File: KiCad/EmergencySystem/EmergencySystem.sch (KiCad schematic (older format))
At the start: 15 parts, among them K1 HE1AN-S-DC12V, K2 HE1AN-S-DC12V, M1 Left_Motor, M2 Right_Motor, U1 T3_EmergencyLight_RED, U2 T3_EmergencyLight_BLUE, U3 T3_EmergencyLight_AMBER, U4 e-Boot_BuckConverter, U5 Elegoo_4RelayModule, U6 Feather_32u4_RFM95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

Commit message: Finalized the initial version of the emergency transmitter/receiver schematic. PDF export was also uploaded.
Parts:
- removed BT1, BT2: Motor_Battery, symbol Device:Battery_Cell
- removed U7: e-Boot_BuckConverter, symbol RoboBoat_Parts:e-Boot_BuckConverter
- added AE1, AE2: Adafruit_900MHz_Antenna, symbol Device:Antenna
- added R1, R2: 5k, symbol Device:R_US
- added SW1: E-StopButton01, symbol Switch:SW_Push_Open
- added SW2: E-StopButton02, symbol Switch:SW_Push_Open
- added SW3, SW4: ON/OFF_Switch, symbol Switch:SW_SPST
- added SW5: E-Stop_Switch, symbol Switch:SW_SPST
- added U10, U7: Adafruit_2200mAh_LiPo, symbol RoboBoat_Parts:Adafruit_2200mAh_LiPo
- added U11: OLED_I2C_Display, symbol RoboBoat_Parts:OLED_I2C_Display
- added U8: Feather_32u4_RFM95, symbol AdafruitBoards:Feather_32u4_RFM95
- added U9: e-Boot_BuckConverter, symbol RoboBoat_Parts:e-Boot_BuckConverter
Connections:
- net labels added: +12V, +3V3_Rx, +3V3_Tx, +5V_Rx, +BATT_14.8V, +BATT_22.2V, -BATT_22.2V, -BATT__14.8V, GND_Rx, GND_Tx, Rx_BatteryMonitor, Tx_BatteryMonitor
- net labels removed: +5V, +BATT, -BATT, GND
- wire segments 81 -> 144
- no-connect marks 16 -> 53
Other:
- note added: "Emergency Receiver"
- note added: "Emergency Transmitter"
- note removed: "22.2V 5S LiPO"
- moved on the sheet: CB1, CB2, K1, K2, M1, M2, U1, U2, U3, U4, U5, U6

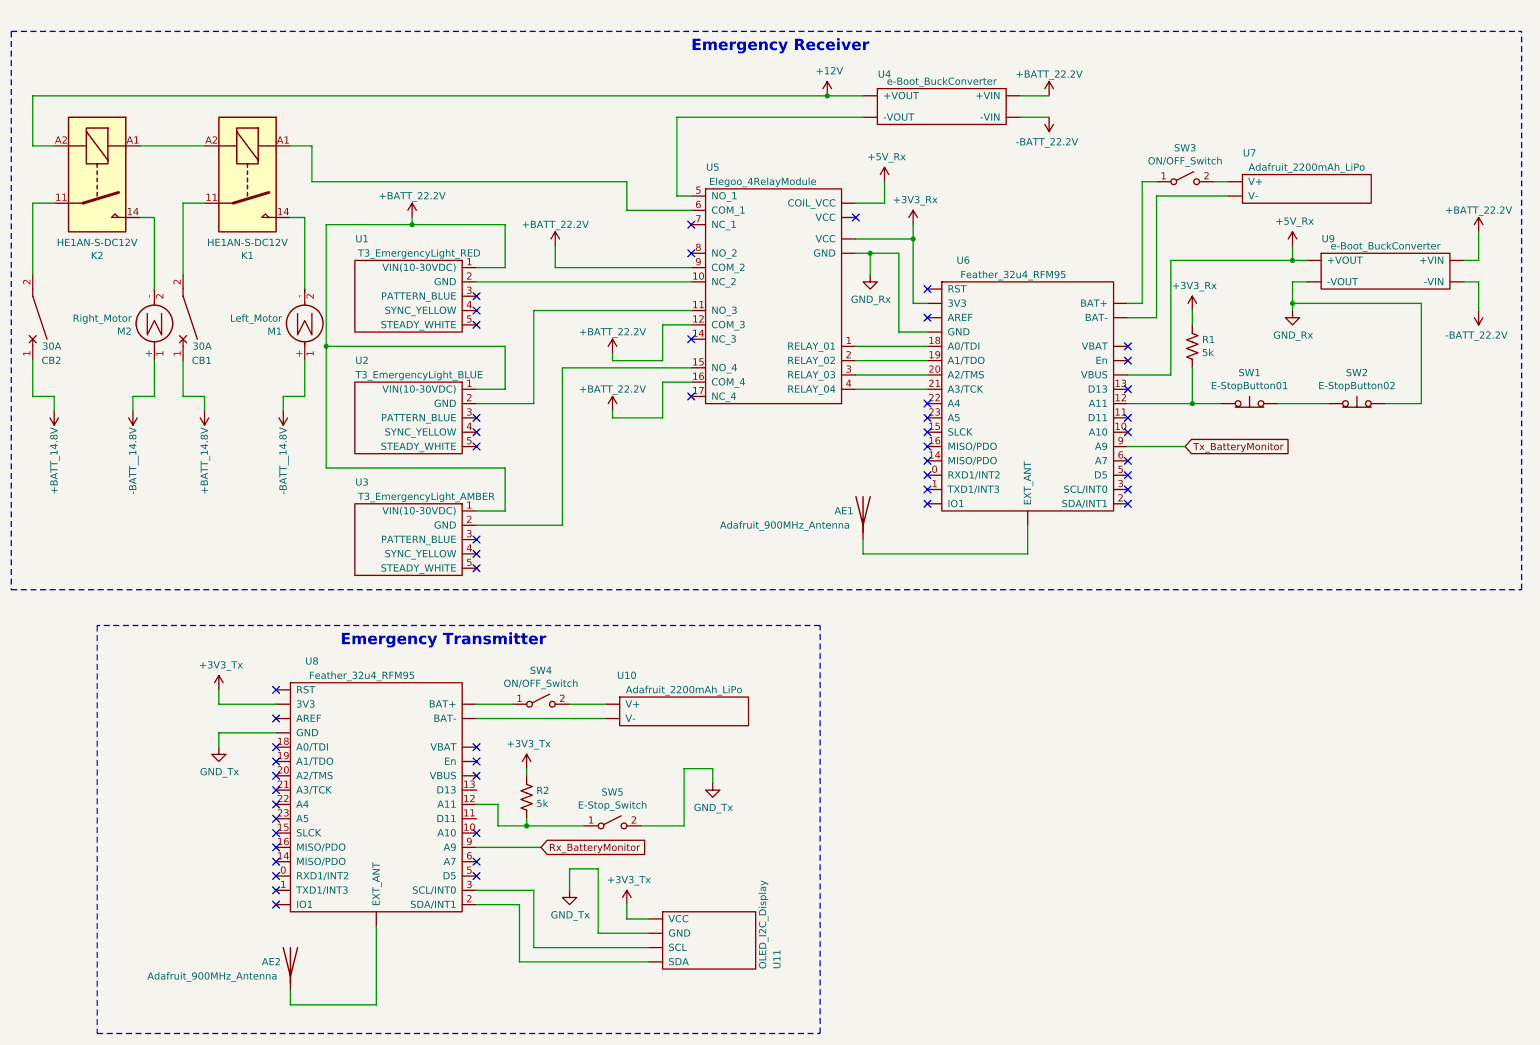
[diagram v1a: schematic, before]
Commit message: Fixed symbol naming issues
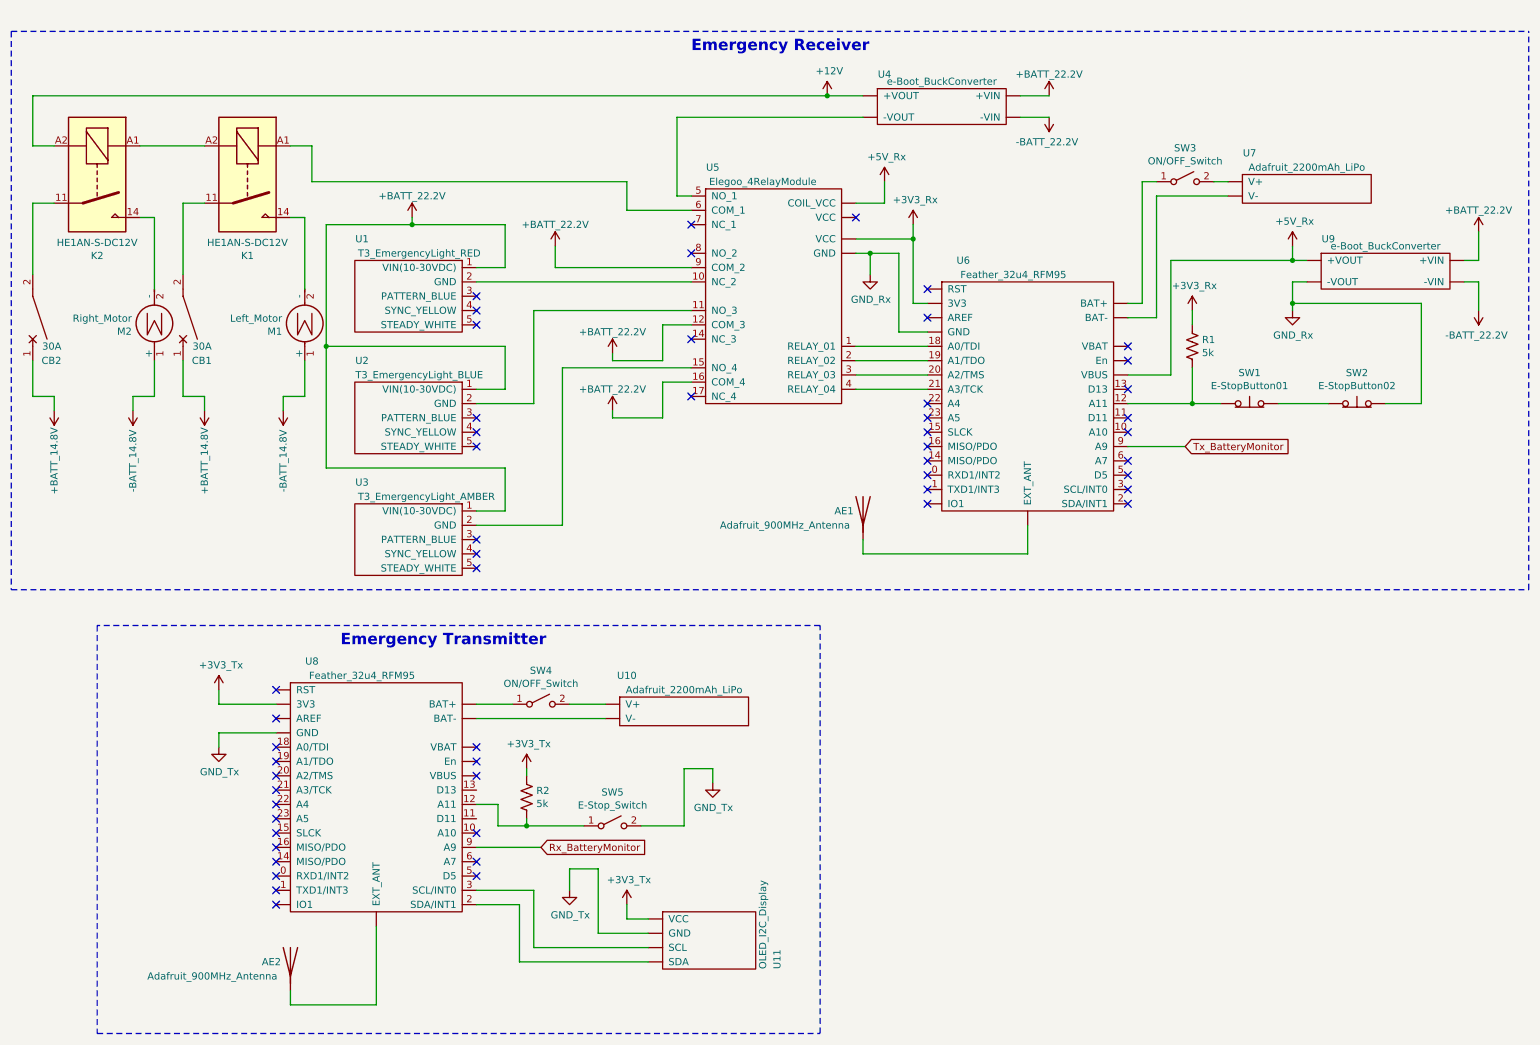
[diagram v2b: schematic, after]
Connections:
- net at U7.~ (V-): now also SW3.2 (B); no longer U6.~ (EXT_ANT)
- net at U10.~ (V-): now also SW4.2 (B); no longer U8.~ (EXT_ANT)
- new net: U6.~ (EXT_ANT), U7.~ (V-)
- new net: U10.~ (V-), U8.~ (EXT_ANT)
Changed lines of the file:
@@
 Wire Wire Line
 	2450 3200 2450 3100
-$Comp
-L RoboBoat_PowerSymbols:-BATT__14.8V #PWR01
-U 1 1 5E597989
-P 2450 3200
-F 0 "#PWR01" H 2450 3050 50  0001 C CNN
-F 1 "-BATT__14.8V" V 2450 3550 50  0000 C CNN
-F 2 "" H 2450 3200 50  0001 C CNN
-F 3 "" H 2450 3200 50  0001 C CNN
-	1    2450 3200
-	-1   0    0    1
-$EndComp
 Wire Wire Line
 	1900 3100 1750 3100
@@
 $EndComp
 $Comp
-L RoboBoat_PowerSymbols:-BATT__14.8V #PWR02
-U 1 1 5E7F616E
-P 1400 3200
-F 0 "#PWR02" H 1400 3050 50  0001 C CNN
-F 1 "-BATT__14.8V" V 1400 3550 50  0000 C CNN
-F 2 "" H 1400 3200 50  0001 C CNN
-F 3 "" H 1400 3200 50  0001 C CNN
-	1    1400 3200
-	-1   0    0    1
-$EndComp
-$Comp
 L RoboBoat_PowerSymbols:+BATT_14.8V #PWR03
 U 1 1 5E7F6561
@@
 	550  550  550  4450
 Wire Notes Line
-	11100 4450 11100 550
-Wire Notes Line
-	550  4450 11100 4450
-Wire Notes Line
-	550  550  11100 550
+	11150 4450 11150 550
 Text Notes 5300 700  0    79   ~ 16
 Emergency Receiver
@@
 NoConn ~ 8350 2850
 NoConn ~ 8350 2750
+Wire Notes Line
+	550  550  11150 550
+Wire Notes Line
+	550  4450 11150 4450
+$Comp
+L RoboBoat_PowerSymbols:-BATT_14.8V #PWR?
+U 1 1 5E41AB6C
+P 1400 3200
+F 0 "#PWR?" H 1400 3050 50  0001 C CNN
+F 1 "-BATT_14.8V" V 1400 3550 50  0000 C CNN
+F 2 "" H 1400 3200 50  0001 C CNN
+F 3 "" H 1400 3200 50  0001 C CNN
+	1    1400 3200
+	-1   0    0    1
+$EndComp
+$Comp
+L RoboBoat_PowerSymbols:-BATT_14.8V #PWR?
+U 1 1 5E41B5C1
+P 2450 3200
+F 0 "#PWR?" H 2450 3050 50  0001 C CNN
+F 1 "-BATT_14.8V" V 2450 3550 50  0000 C CNN
+F 2 "" H 2450 3200 50  0001 C CNN
+F 3 "" H 2450 3200 50  0001 C CNN
+	1    2450 3200
+	-1   0    0    1
+$EndComp
 $EndSCHEMATC

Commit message: Added Ultimate GPS to the Teensy Schematic and updated our custom symbol library
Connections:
- net at U7.~ (V-): now also SW3.2 (B); no longer U6.~ (EXT_ANT)
- net at U10.~ (V-): now also SW4.2 (B); no longer U8.~ (EXT_ANT)
- new net: U6.~ (EXT_ANT), U7.~ (V-)
- new net: U10.~ (V-), U8.~ (EXT_ANT)
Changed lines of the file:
@@
 $EndComp
 $Comp
-L RoboBoat_PowerSymbols:+3V3_Rx #PWR022
+L EmergencySystem-rescue:+3V3_Rx-RoboBoat_PowerSymbols #PWR022
 U 1 1 5E3ED7E6
 P 6850 1900
@@
 $EndComp
 $Comp
-L RoboBoat_PowerSymbols:+3V3_Rx #PWR025
+L EmergencySystem-rescue:+3V3_Rx-RoboBoat_PowerSymbols #PWR025
 U 1 1 5E3EDF11
 P 8800 2500
@@
 	550  4450 11150 4450
 $Comp
-L RoboBoat_PowerSymbols:-BATT_14.8V #PWR?
+L RoboBoat_PowerSymbols:-BATT_14.8V #PWR01
 U 1 1 5E41AB6C
 P 1400 3200
-F 0 "#PWR?" H 1400 3050 50  0001 C CNN
+F 0 "#PWR01" H 1400 3050 50  0001 C CNN
 F 1 "-BATT_14.8V" V 1400 3550 50  0000 C CNN
 F 2 "" H 1400 3200 50  0001 C CNN
@@
 $EndComp
 $Comp
-L RoboBoat_PowerSymbols:-BATT_14.8V #PWR?
+L RoboBoat_PowerSymbols:-BATT_14.8V #PWR02
 U 1 1 5E41B5C1
 P 2450 3200
-F 0 "#PWR?" H 2450 3050 50  0001 C CNN
+F 0 "#PWR02" H 2450 3050 50  0001 C CNN
 F 1 "-BATT_14.8V" V 2450 3550 50  0000 C CNN
 F 2 "" H 2450 3200 50  0001 C CNN
